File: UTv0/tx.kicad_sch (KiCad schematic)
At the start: 0 parts

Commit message: Transmit Circuit
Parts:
- added C?: 100nF, symbol Device:C
- added C?: 20uF, 200V, symbol Device:C
- added C? (x2): 100nF, 200V, symbol Device:C
- added C?: 0.1uF, symbol Device:C
- added C?: 4.7uF, symbol Device:C
- added C?: 50pF, symbol Device:C
- added C?: 1nF, symbol Device:C
- added C?: 47uF, symbol Device:C
- added J?: C5, symbol Connector:Conn_Coaxial
- added Q?: IRL620, symbol Simulation_SPICE:NMOS
- added R?: 10K, symbol Device:R
- added R?: 50, symbol Device:R
- added R?: 10K, symbol Device:R_Variable
- added R?: 3K, symbol Device:R
- added U?: LM7805_TO220, Package_TO_SOT_THT:TO-220-3_Vertical, symbol Regulator_Linear:LM7805_TO220
- added U?: 74LS121, symbol 74xx:74LS121
- added U?: ICL7667, symbol Driver_FET:ICL7667
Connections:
- new net: Q?.2 (G), R?.1, U?.5 (~{OUTB}), U?.7 (~{OUTA})
- new net: C?.1, U?.10 (Cext)
- new net: C?.2, U?.11 (R/Cext)
- new net: R?.2, U?.9 (Rint)
- new net: C?.2, J?.1 (In), R?.1
- new net: C?.1, Q?.1 (D), R?.2
- new net +100V: C?.2, C?.2, R?.1
- new net +5V: C?.2, R?.1, U?.1 (~{Q}), U?.14 (VCC), U?.2 (INA), U?.3 (VO), U?.4 (INB)
- new net +9V: C?.2, C?.2, C?.2, U?.1 (VI), U?.6 (V+)
- new net GND: C?.1, C?.1, C?.1, C?.1, C?.1, C?.1, C?.1, J?.2 (Ext), Q?.3 (S), R?.2, R?.2, U?.2 (GND), U?.3 (A1), U?.3 (V-), U?.4 (A2), U?.7 (GND)
- new net Trig: C?.2, U?.5 (B)
- no-connect marks 0 -> 2
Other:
- note added: "-100V"
- note added: "0V"
- note added: "9V"

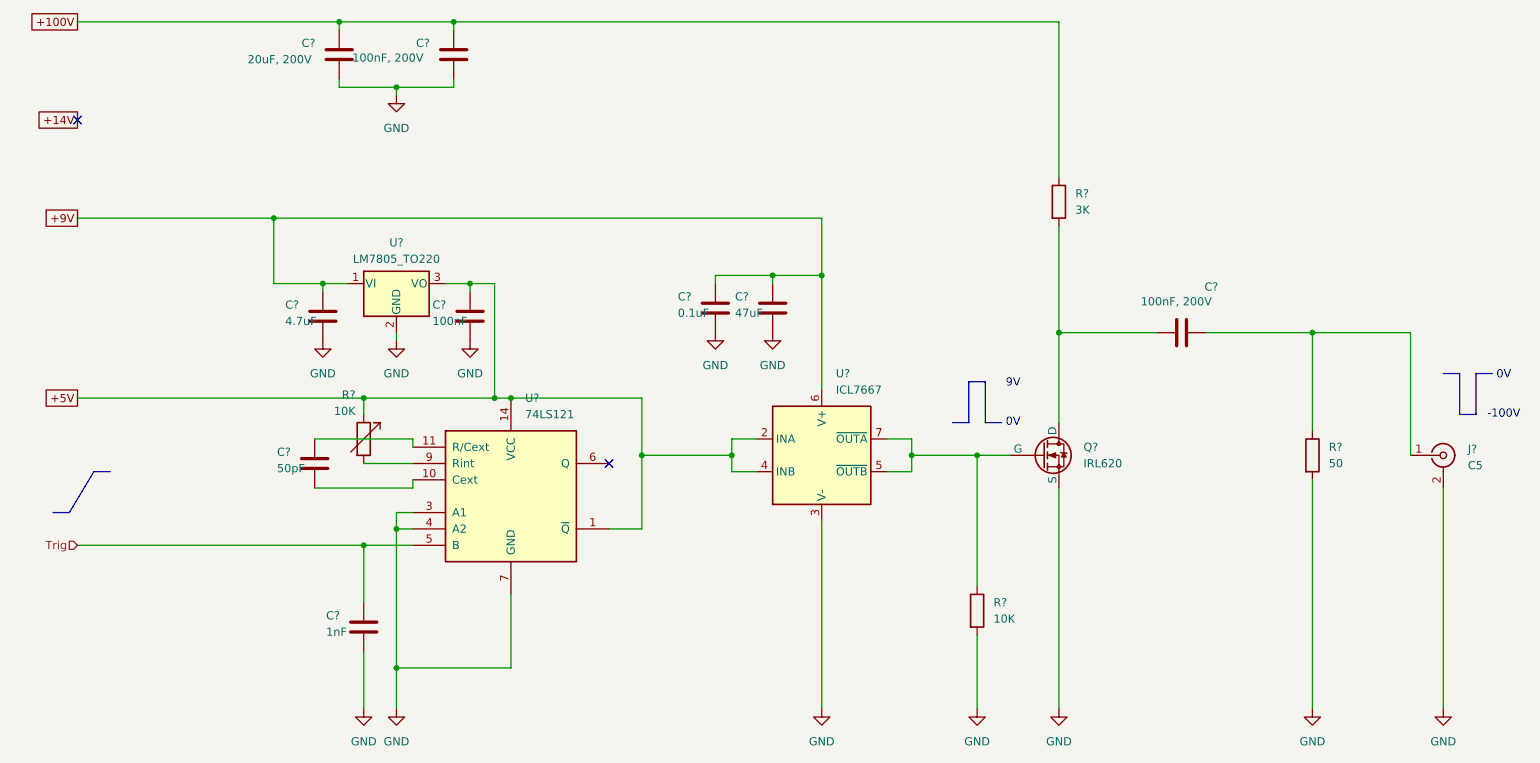
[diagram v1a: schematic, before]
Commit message: Schematic revised, initial tests started
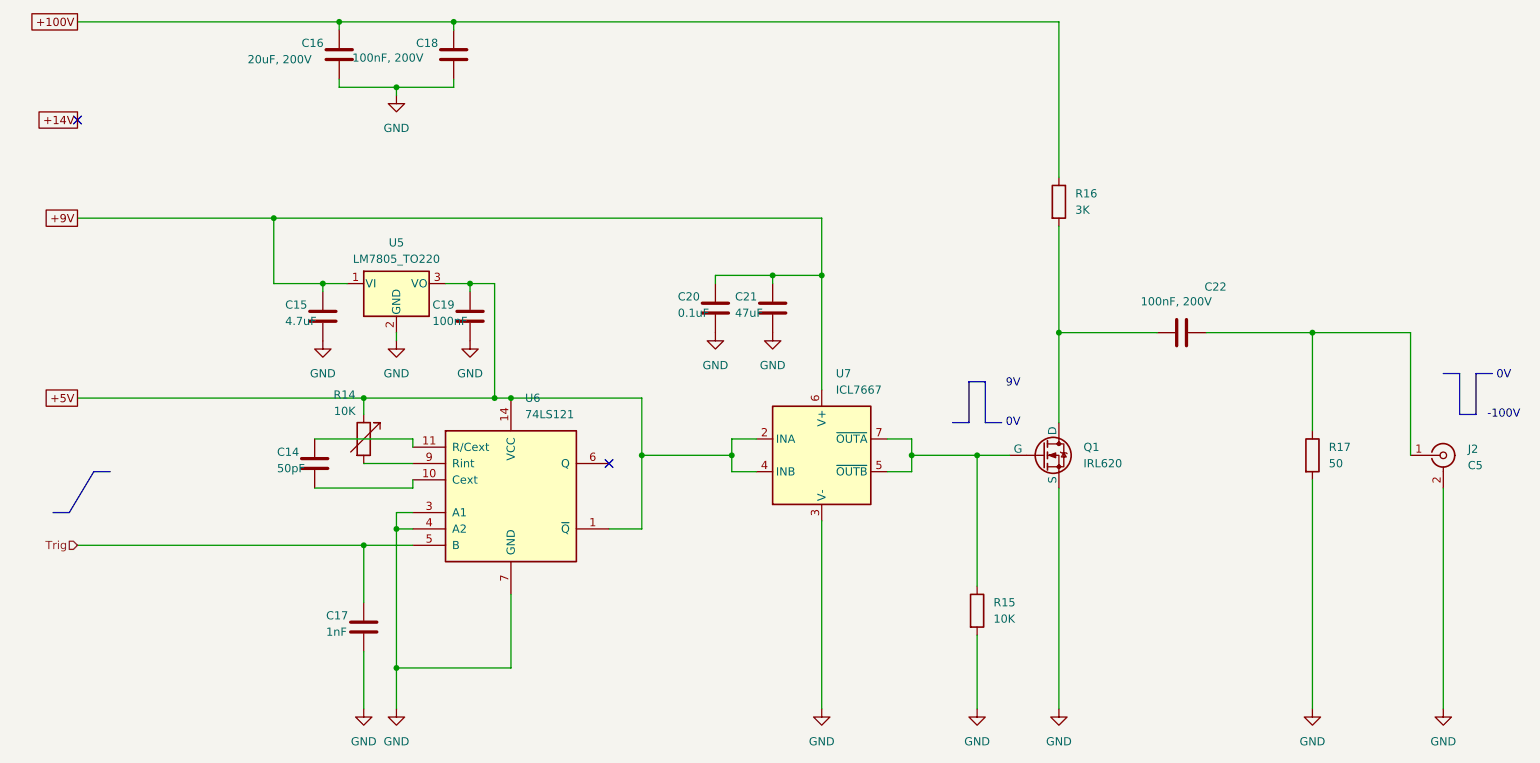
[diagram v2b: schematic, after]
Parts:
- gave numbers to parts that had none: 18
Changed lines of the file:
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@@
 		(dnp no)
 		(fields_autoplaced yes)
-		(property "Reference" "U?"
+		(property "Reference" "U5"
 			(at 96.52 72.39 0)
 			(effects
@@
 			(project ""
 				(path "/bd24c4db-4e36-4117-bd4f-5228ef241da9/347c3b27-5569-44f0-9bfc-0cdf1d200bc1"
-					(reference "U?")
+					(reference "U5")
 					(unit 1)
 				)
@@
 		(on_board yes)
 		(dnp no)
-		(property "Reference" "C?"
+		(property "Reference" "C19"
 			(at 102.108 82.042 0)
 			(effects
@@
 			(project "UTv0"
 				(path "/bd24c4db-4e36-4117-bd4f-5228ef241da9/347c3b27-5569-44f0-9bfc-0cdf1d200bc1"
-					(reference "C?")
+					(reference "C19")
 					(unit 1)
 				)
@@
 		(dnp no)
 		(fields_autoplaced yes)
-		(property "Reference" "R?"
+		(property "Reference" "R15"
 			(at 189.23 128.2699 0)
 			(effects
@@
 			(project "UTv0"
 				(path "/bd24c4db-4e36-4117-bd4f-5228ef241da9/347c3b27-5569-44f0-9bfc-0cdf1d200bc1"
-					(reference "R?")
+					(reference "R15")
 					(unit 1)
 				)
@@
 		(on_board yes)
 		(dnp no)
-		(property "Reference" "C?"
+		(property "Reference" "C16"
 			(at 81.788 41.402 0)
 			(effects
@@
 			(project "UTv0"
 				(path "/bd24c4db-4e36-4117-bd4f-5228ef241da9/347c3b27-5569-44f0-9bfc-0cdf1d200bc1"
-					(reference "C?")
+					(reference "C16")
 					(unit 1)
 				)
@@
 		(dnp no)
 		(fields_autoplaced yes)
-		(property "Reference" "U?"
+		(property "Reference" "U6"
 			(at 116.4941 96.52 0)
 			(effects
@@
 			(project ""
 				(path "/bd24c4db-4e36-4117-bd4f-5228ef241da9/347c3b27-5569-44f0-9bfc-0cdf1d200bc1"
-					(reference "U?")
+					(reference "U6")
 					(unit 1)
 				)
@@
 		(on_board yes)
 		(dnp no)
-		(property "Reference" "C?"
+		(property "Reference" "C18"
 			(at 99.568 41.402 0)
 			(effects
@@
 			(project "UTv0"
 				(path "/bd24c4db-4e36-4117-bd4f-5228ef241da9/347c3b27-5569-44f0-9bfc-0cdf1d200bc1"
-					(reference "C?")
+					(reference "C18")
 					(unit 1)
 				)
@@
 		(dnp no)
 		(fields_autoplaced yes)
-		(property "Reference" "R?"
+		(property "Reference" "R17"
 			(at 241.3 104.1399 0)
 			(effects
@@
 			(project "UTv0"
 				(path "/bd24c4db-4e36-4117-bd4f-5228ef241da9/347c3b27-5569-44f0-9bfc-0cdf1d200bc1"
-					(reference "R?")
+					(reference "R17")
 					(unit 1)
 				)
@@
 		(on_board yes)
 		(dnp no)
-		(property "Reference" "R?"
+		(property "Reference" "R14"
 			(at 90.17 96.012 0)
 			(effects
@@
 			(project "UTv0"
 				(path "/bd24c4db-4e36-4117-bd4f-5228ef241da9/347c3b27-5569-44f0-9bfc-0cdf1d200bc1"
-					(reference "R?")
+					(reference "R14")
 					(unit 1)
 				)
@@
 		(on_board yes)
 		(dnp no)
-		(property "Reference" "C?"
+		(property "Reference" "C20"
 			(at 140.208 80.772 0)
 			(effects
@@
 			(project "UTv0"
 				(path "/bd24c4db-4e36-4117-bd4f-5228ef241da9/347c3b27-5569-44f0-9bfc-0cdf1d200bc1"
-					(reference "C?")
+					(reference "C20")
 					(unit 1)
 				)
@@
 		(dnp no)
 		(fields_autoplaced yes)
-		(property "Reference" "J?"
+		(property "Reference" "J2"
 			(at 262.89 104.4331 0)
 			(effects
@@
 			(project "UTv0"
 				(path "/bd24c4db-4e36-4117-bd4f-5228ef241da9/347c3b27-5569-44f0-9bfc-0cdf1d200bc1"
-					(reference "J?")
+					(reference "J2")
 					(unit 1)
 				)
@@
 		(dnp no)
 		(fields_autoplaced yes)
-		(property "Reference" "U?"
+		(property "Reference" "U7"
 			(at 164.7541 92.71 0)
 			(effects
@@
 			(project ""
 				(path "/bd24c4db-4e36-4117-bd4f-5228ef241da9/347c3b27-5569-44f0-9bfc-0cdf1d200bc1"
-					(reference "U?")
+					(reference "U7")
 					(unit 1)
 				)
@@
 		(on_board yes)
 		(dnp no)
-		(property "Reference" "C?"
+		(property "Reference" "C22"
 			(at 221.996 79.248 90)
 			(effects
@@
 			(project "UTv0"
 				(path "/bd24c4db-4e36-4117-bd4f-5228ef241da9/347c3b27-5569-44f0-9bfc-0cdf1d200bc1"
-					(reference "C?")
+					(reference "C22")
 					(unit 1)
 				)
@@
 		(on_board yes)
 		(dnp no)
-		(property "Reference" "C?"
+		(property "Reference" "C15"
 			(at 79.248 82.042 0)
 			(effects
@@
 			(project "UTv0"
 				(path "/bd24c4db-4e36-4117-bd4f-5228ef241da9/347c3b27-5569-44f0-9bfc-0cdf1d200bc1"
-					(reference "C?")
+					(reference "C15")
 					(unit 1)
 				)
@@
 		(dnp no)
 		(fields_autoplaced yes)
-		(property "Reference" "R?"
+		(property "Reference" "R16"
 			(at 201.93 64.7699 0)
 			(effects
@@
 			(project "UTv0"
 				(path "/bd24c4db-4e36-4117-bd4f-5228ef241da9/347c3b27-5569-44f0-9bfc-0cdf1d200bc1"
-					(reference "R?")
+					(reference "R16")
 					(unit 1)
 				)
@@
 		(on_board yes)
 		(dnp no)
-		(property "Reference" "C?"
+		(property "Reference" "C14"
 			(at 77.978 104.902 0)
 			(effects
@@
 			(project "UTv0"
 				(path "/bd24c4db-4e36-4117-bd4f-5228ef241da9/347c3b27-5569-44f0-9bfc-0cdf1d200bc1"
-					(reference "C?")
+					(reference "C14")
 					(unit 1)
 				)
@@
 		(dnp no)
 		(fields_autoplaced yes)
-		(property "Reference" "Q?"
+		(property "Reference" "Q1"
 			(at 203.2 104.1399 0)
 			(effects
@@
 			(project ""
 				(path "/bd24c4db-4e36-4117-bd4f-5228ef241da9/347c3b27-5569-44f0-9bfc-0cdf1d200bc1"
-					(reference "Q?")
+					(reference "Q1")
 					(unit 1)
 				)
@@
 		(on_board yes)
 		(dnp no)
-		(property "Reference" "C?"
+		(property "Reference" "C17"
 			(at 85.598 130.302 0)
 			(effects
@@
 			(project "UTv0"
 				(path "/bd24c4db-4e36-4117-bd4f-5228ef241da9/347c3b27-5569-44f0-9bfc-0cdf1d200bc1"
-					(reference "C?")
+					(reference "C17")
 					(unit 1)
 				)
@@
 		(on_board yes)
 		(dnp no)
-		(property "Reference" "C?"
+		(property "Reference" "C21"
 			(at 149.098 80.772 0)
 			(effects
@@
 			(project "UTv0"
 				(path "/bd24c4db-4e36-4117-bd4f-5228ef241da9/347c3b27-5569-44f0-9bfc-0cdf1d200bc1"
-					(reference "C?")
-					(unit 1)
-				)
+					(reference "C21")
+					(unit 1)
+				)

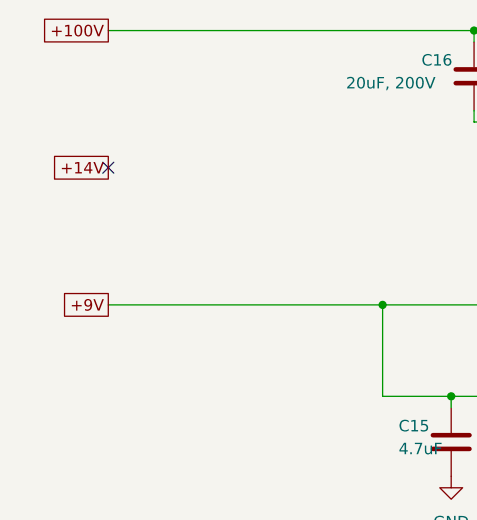
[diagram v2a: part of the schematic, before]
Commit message: v6 cleanup + back to delta (dubious), v7: new methods to detect peak + dynamic reference + thresholding (does not work), backtrack
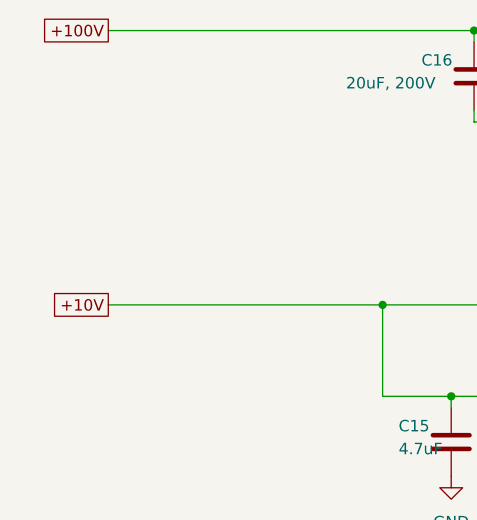
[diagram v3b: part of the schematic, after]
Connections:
- net +9V renamed +10V
- no-connect marks 2 -> 1
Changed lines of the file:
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@@
-	)
-	(no_connect
-		(at 46.99 53.34)
 	)
 	(no_connect
@@
 		)
 	)
-	(global_label "+14V"
-		(shape passive)
-		(at 46.99 53.34 180)
-		(fields_autoplaced yes)
-		(effects
-			(font
-				(size 1.27 1.27)
-			)
-			(justify right)
-		)
-		(property "Intersheetrefs" "${INTERSHEET_REFS}"
-			(at 40.0361 53.34 0)
-			(effects
-				(font
-					(size 1.27 1.27)
-				)
-				(justify right)
-				(hide yes)
-			)
-		)
-	)
-	(global_label "+9V"
+	(global_label "+10V"
 		(shape passive)
 		(at 46.99 68.58 180)
@@
 		)
 		(property "Intersheetrefs" "${INTERSHEET_REFS}"
-			(at 41.2456 68.58 0)
+			(at 40.0361 68.58 0)
 			(effects
 				(font
